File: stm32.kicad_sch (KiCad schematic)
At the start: 20 parts, among them IC1 ADBMS6821CCSZ, J5 Conn_02x03_Top_Bottom, SW3 SW_Nidec_CAS-120A1, T1 74941301, U10 STM32G431RBTx, U15 SN65HVD235, Y2 16 MHz

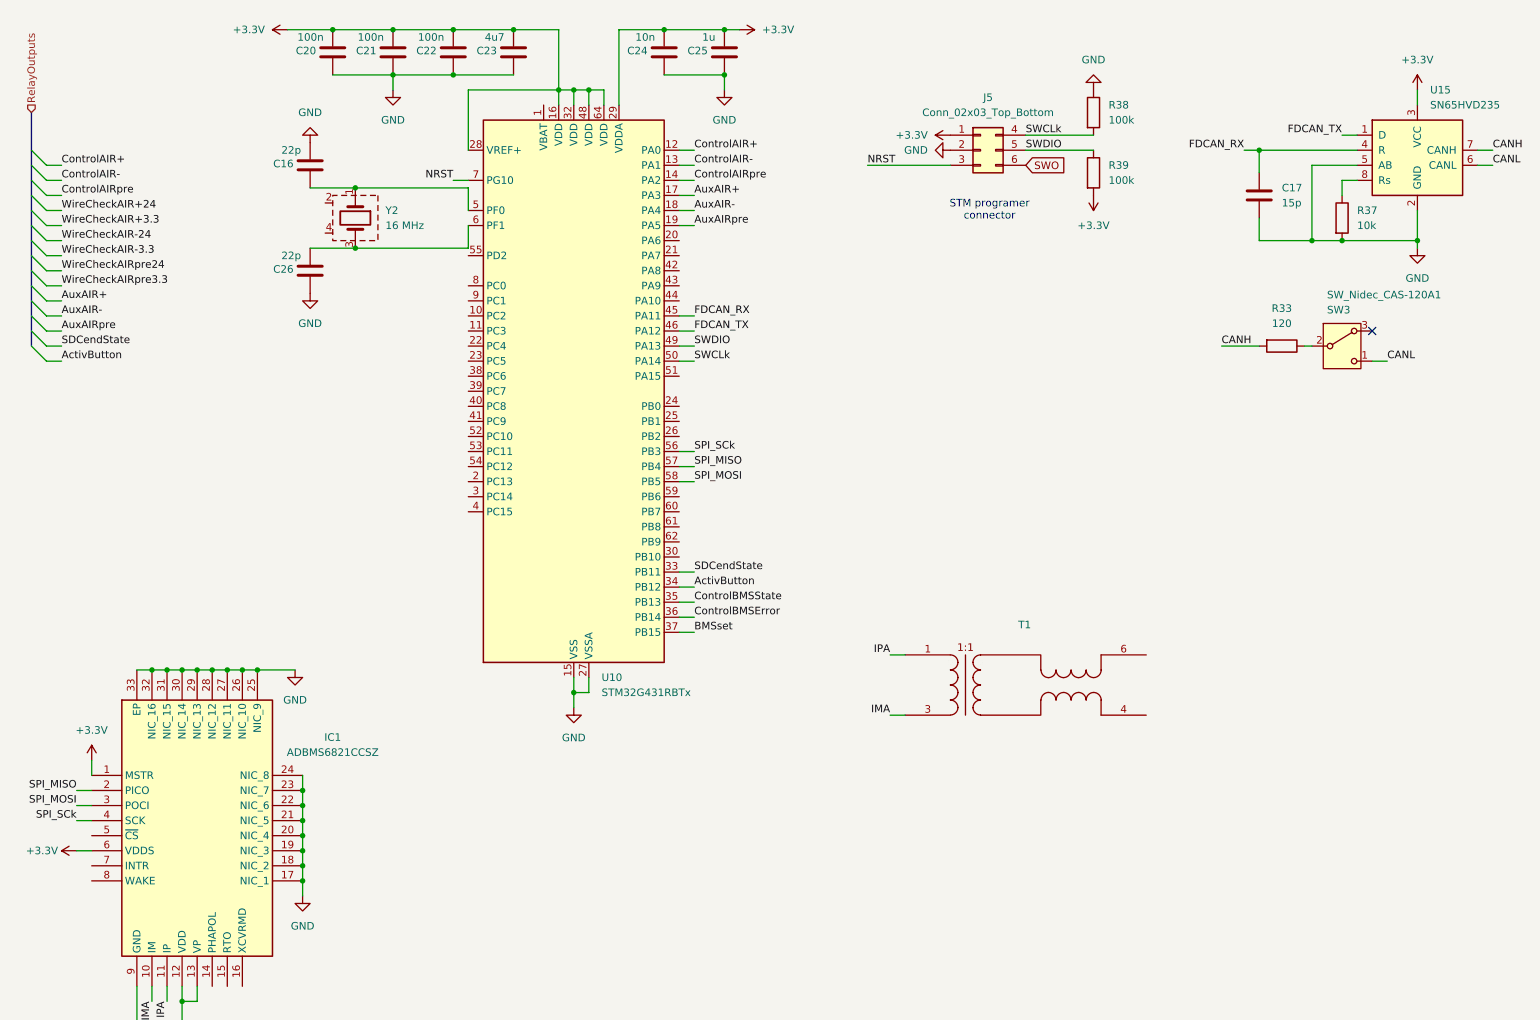
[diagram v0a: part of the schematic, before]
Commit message: Canvi de microcontrolador Control dels relés de potència actualitzat Leds afegits per a visualitzar l'estat del fusible
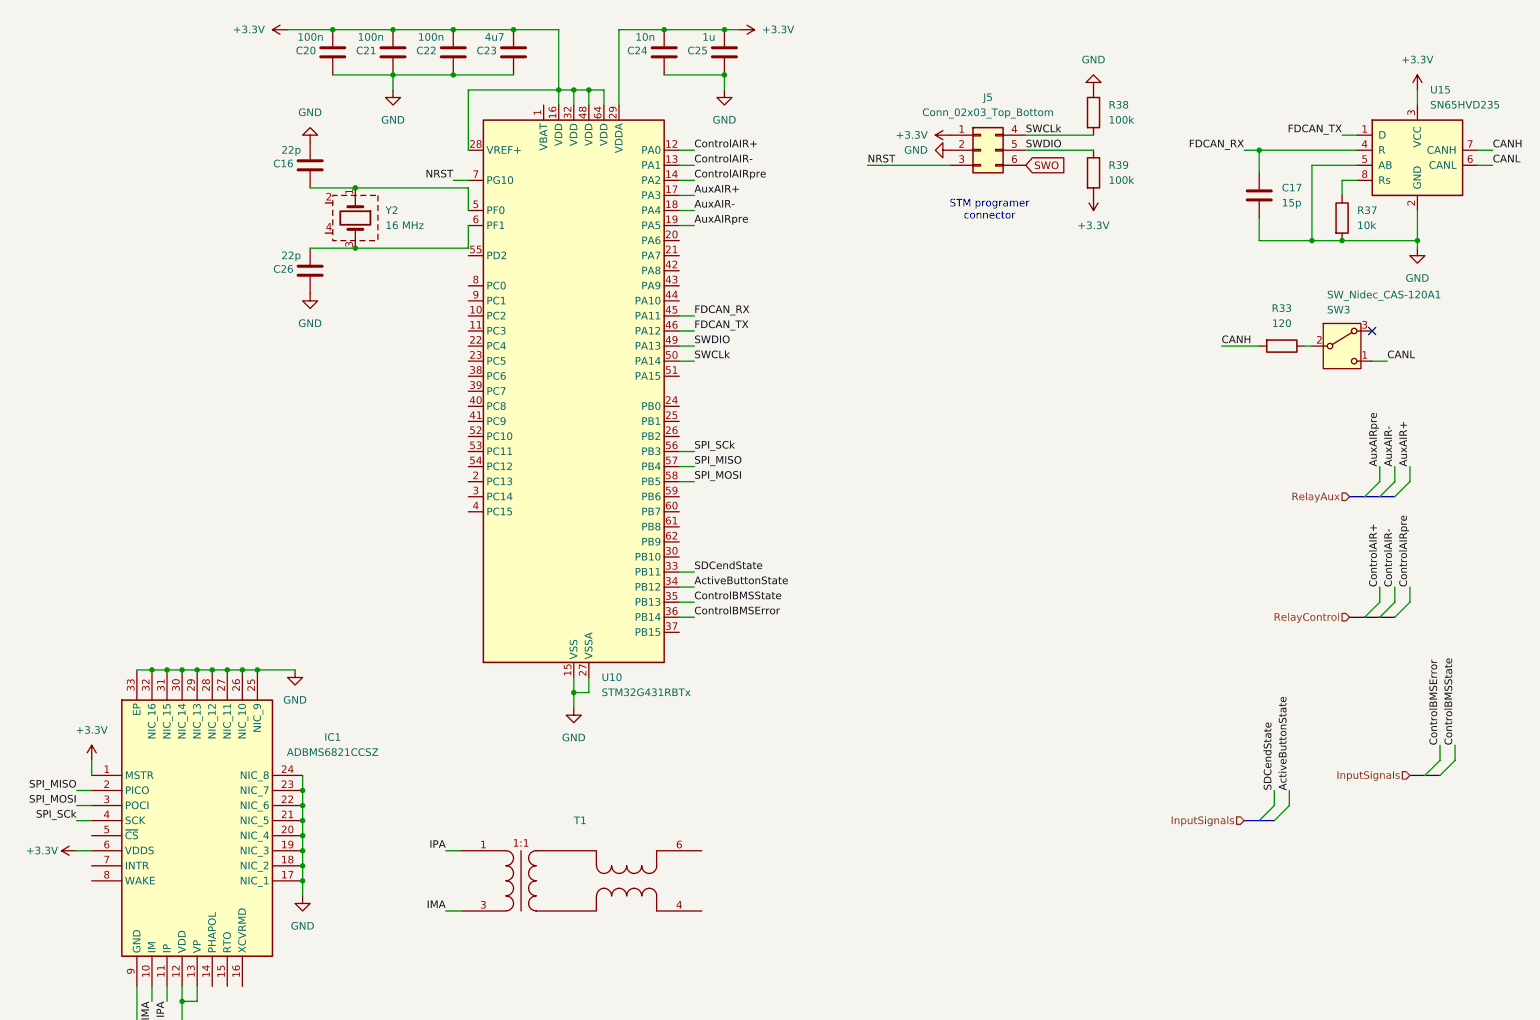
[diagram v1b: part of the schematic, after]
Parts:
- C16, C17, C20, C21, C22, C23, C24, C25, C26: footprint Capacitor_SMD:C_1206_3216Metric -> Capacitor_SMD:C_0603_1608Metric_Pad1.08x0.95mm_HandSolder
- R33, R37, R38, R39: footprint Resistor_SMD:R_1206_3216Metric -> Resistor_SMD:R_0201_0603Metric_Pad0.64x0.40mm_HandSolder
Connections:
- net ActivButton renamed ActiveButtonState
- net BMSset: no longer names the net of U10.37 (PB15)
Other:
- moved on the sheet: T1

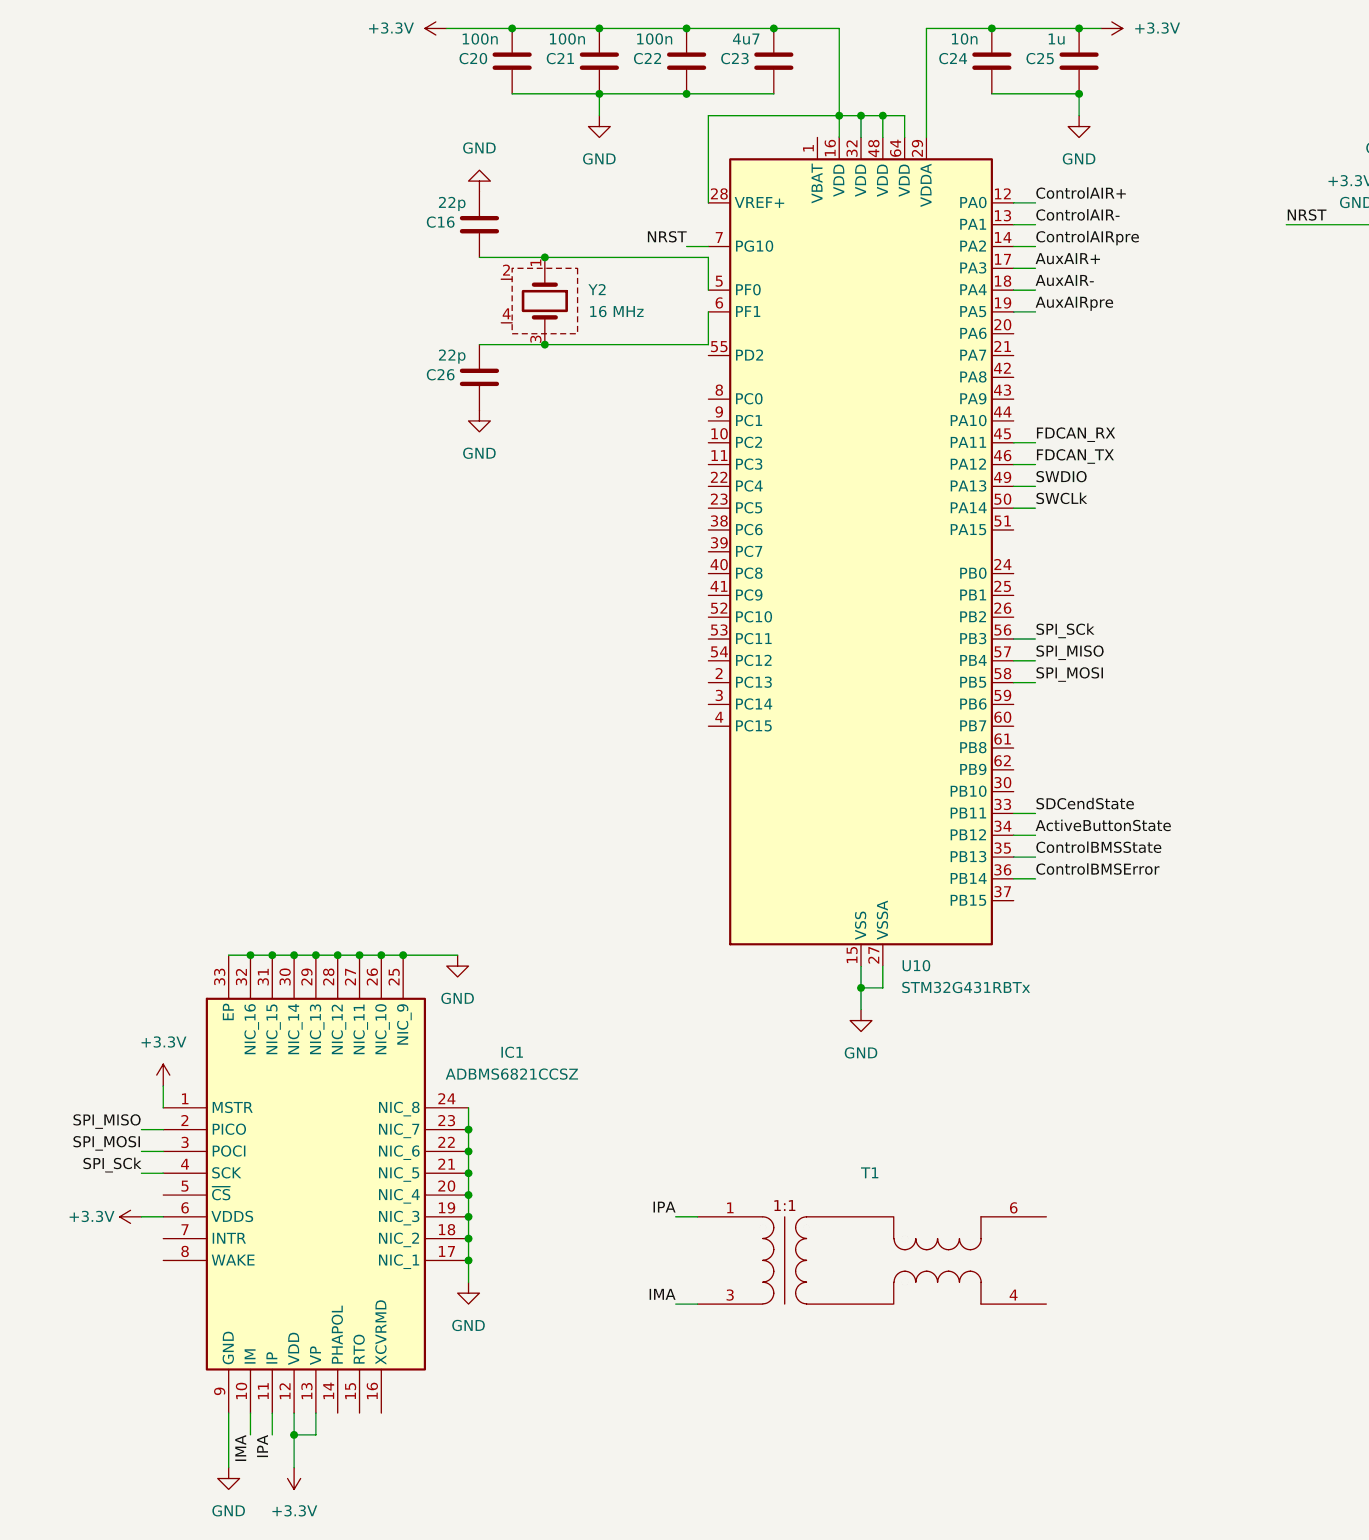
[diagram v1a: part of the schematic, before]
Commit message: - Outputs i inputs del ADBMS6822 acabats de configurar i assignar - TVS eliminat del circuit de descàrrega dels AIRs
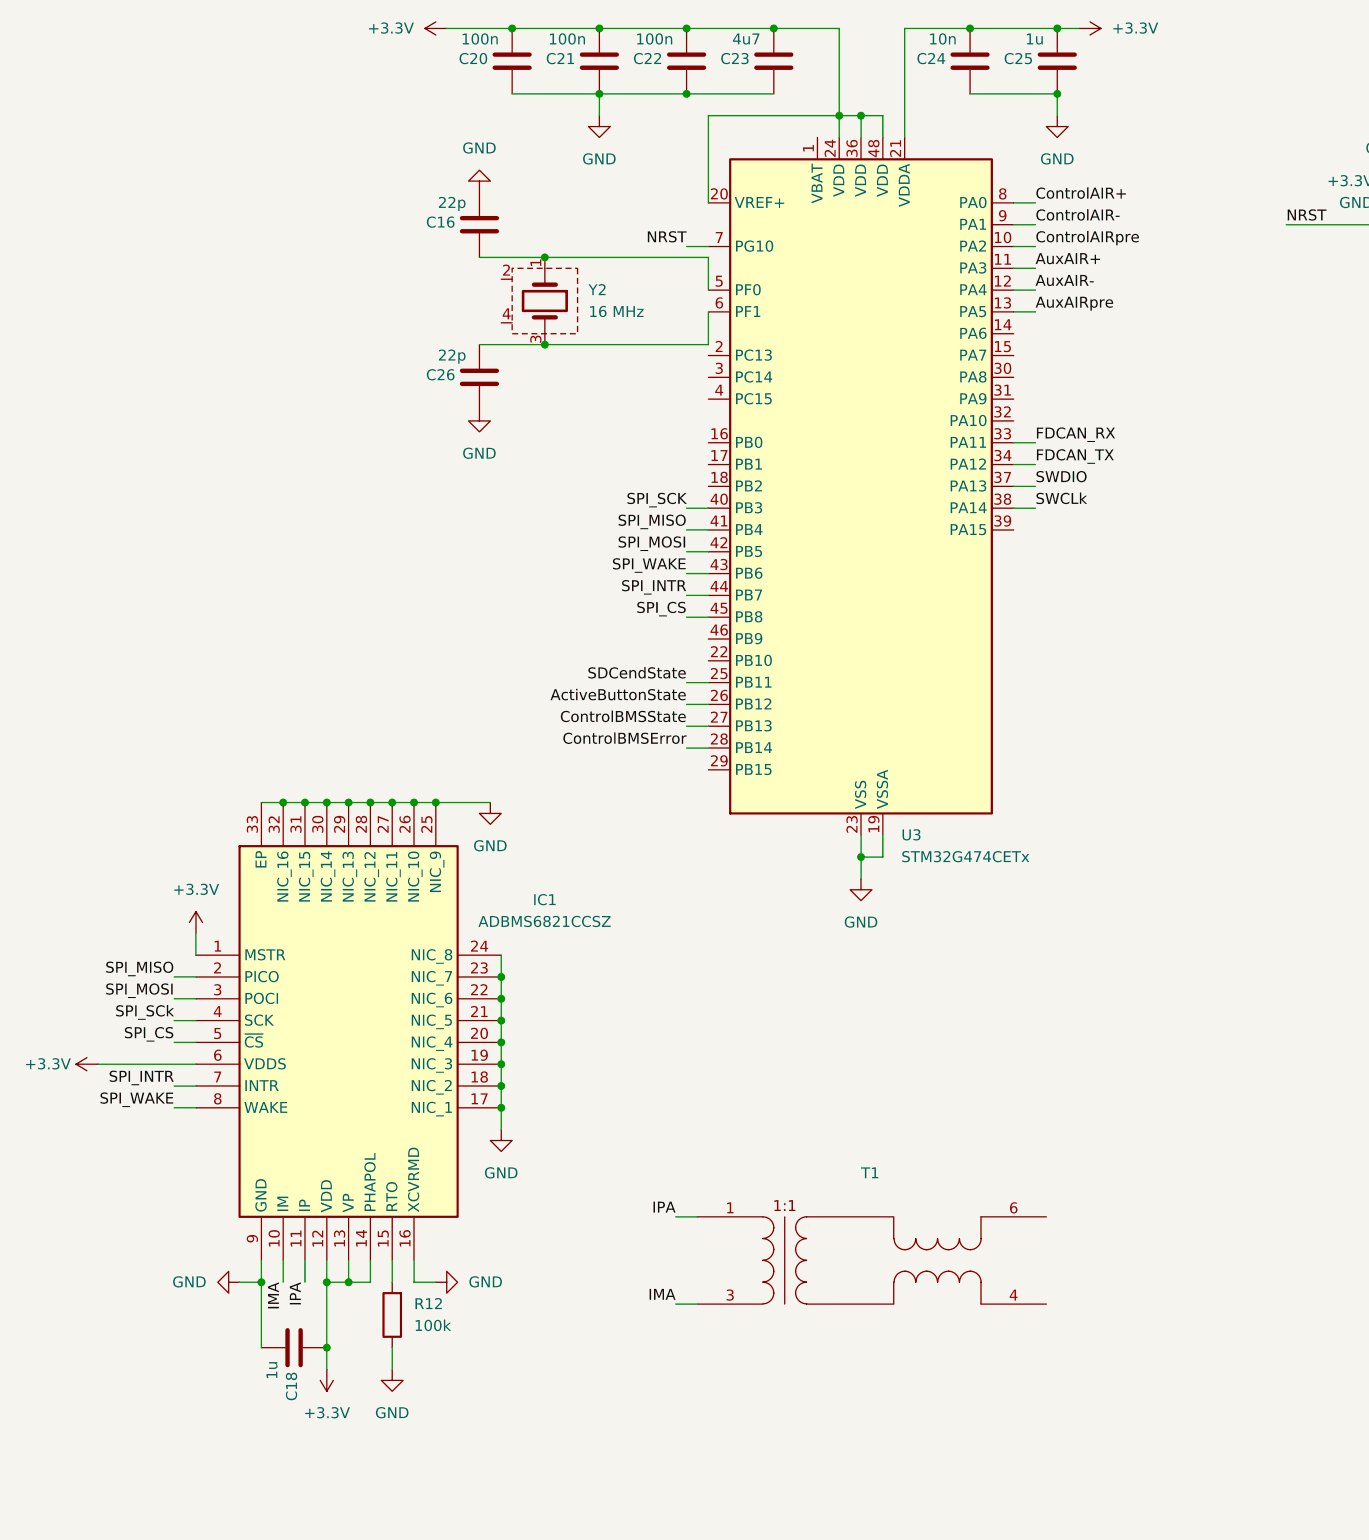
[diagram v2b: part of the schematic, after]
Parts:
- removed U10: STM32G431RBTx, Package_QFP:LQFP-64_10x10mm_P0.5mm, symbol MCU_ST_STM32G4:STM32G431RBTx
- added C18: 1u, Capacitor_SMD:C_0603_1608Metric_Pad1.08x0.95mm_HandSolder, symbol Device:C
- added R12: 100k, Resistor_SMD:R_0201_0603Metric_Pad0.64x0.40mm_HandSolder, symbol Device:R
- added U3: STM32G474CETx, Package_QFP:LQFP-48_7x7mm_P0.5mm, symbol MCU_ST_STM32G4:STM32G474CETx
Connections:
- net +3.3V: now also IC1.14 (PHAPOL), C18.1, U3.20 (VREF+), U3.21 (VDDA), U3.24 (VDD), U3.36 (VDD), U3.48 (VDD)
- net ActiveButtonState: now also U3.26 (PB12)
- net AuxAIR+: now also U3.11 (PA3)
- net AuxAIR-: now also U3.12 (PA4)
- net AuxAIRpre: now also U3.13 (PA5)
- net ControlAIR+: now also U3.8 (PA0)
- net ControlAIR-: now also U3.9 (PA1)
- net ControlAIRpre: now also U3.10 (PA2)
- net ControlBMSError: now also U3.28 (PB14)
- net ControlBMSState: now also U3.27 (PB13)
- net FDCAN_RX: now also U3.33 (PA11)
- net FDCAN_TX: now also U3.34 (PA12)
- net GND: now also IC1.16 (XCVRMD), C18.2, R12.1, U3.19 (VSSA), U3.23 (VSS), U3.35 (VSS), U3.47 (VSS)
- net NRST: now also U3.7 (PG10)
- net SDCendState: now also U3.25 (PB11)
- net SPI_MISO: now also U3.41 (PB4)
- net SPI_MOSI: now also U3.42 (PB5)
- net SWCLk: now also U3.38 (PA14)
- net SWDIO: now also U3.37 (PA13)
- net at C26.2, Y2.3: now also U3.6 (PF1)
- net at C16.1, Y2.1: now also U3.5 (PF0)
- net at IC1.15 (RTO): now also R12.2
- net SPI_CS: now reaches IC1.5 (~{CS})
- net SPI_CS: now also U3.45 (PB8)
- net SPI_INTR: now reaches IC1.7 (INTR)
- net SPI_INTR: now also U3.44 (PB7)
- net SPI_WAKE: now reaches IC1.8 (WAKE)
- net SPI_WAKE: now also U3.43 (PB6)
- new net SPI_SCK: U3.40 (PB3)
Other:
- moved on the sheet: C24, C25, IC1
